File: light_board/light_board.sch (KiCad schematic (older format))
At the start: 15 parts, among them J1 CONN_01x02, Q1 PFET, U1 LM3409MY

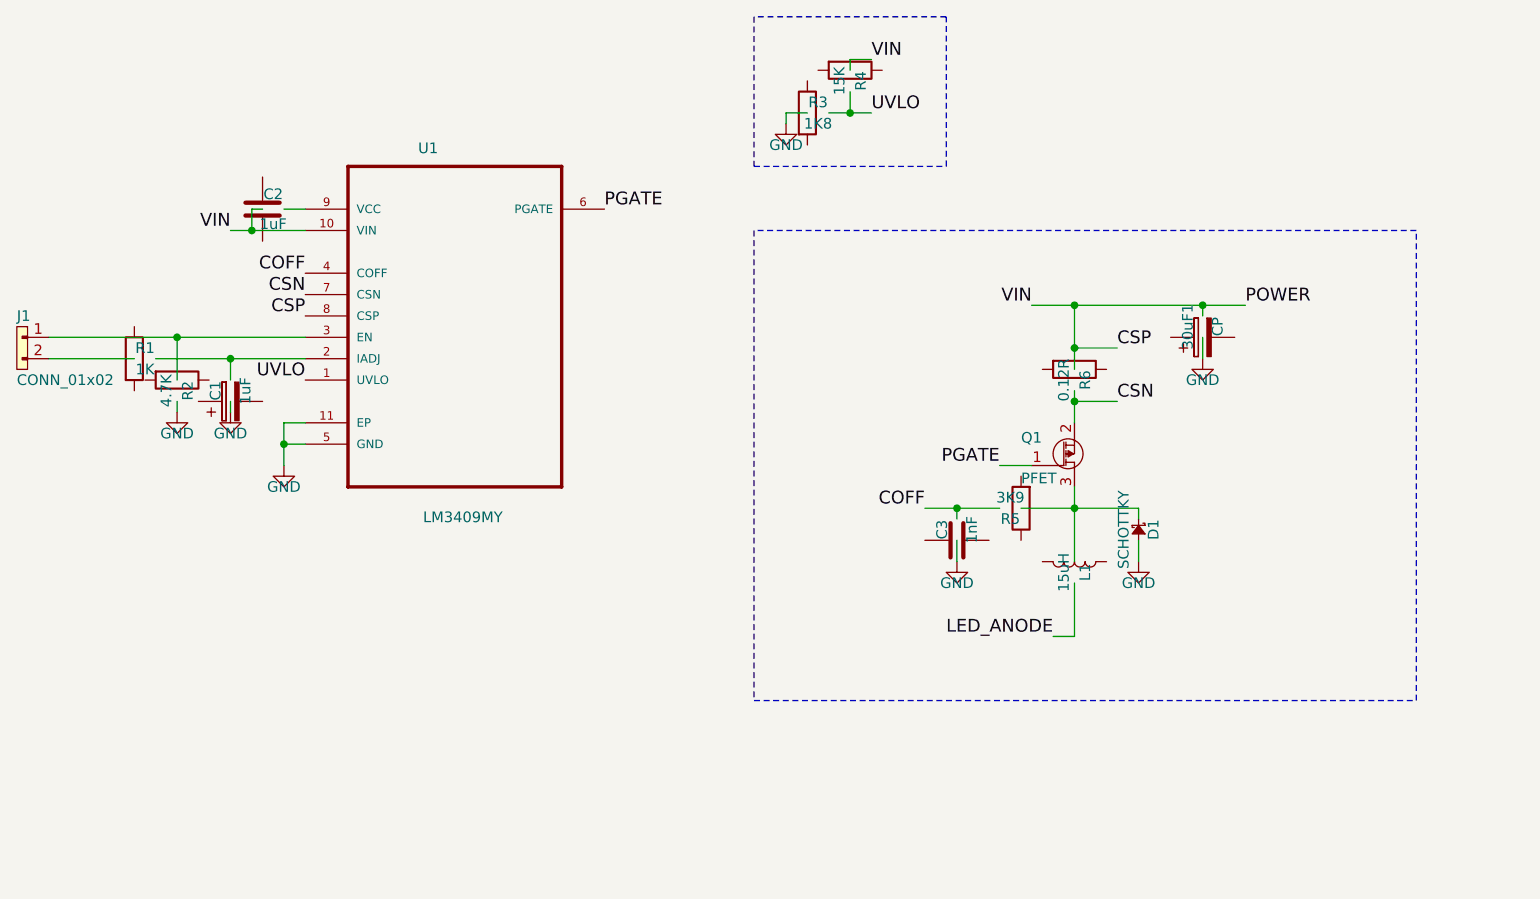
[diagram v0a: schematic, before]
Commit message: first version of light board, need to change resistor
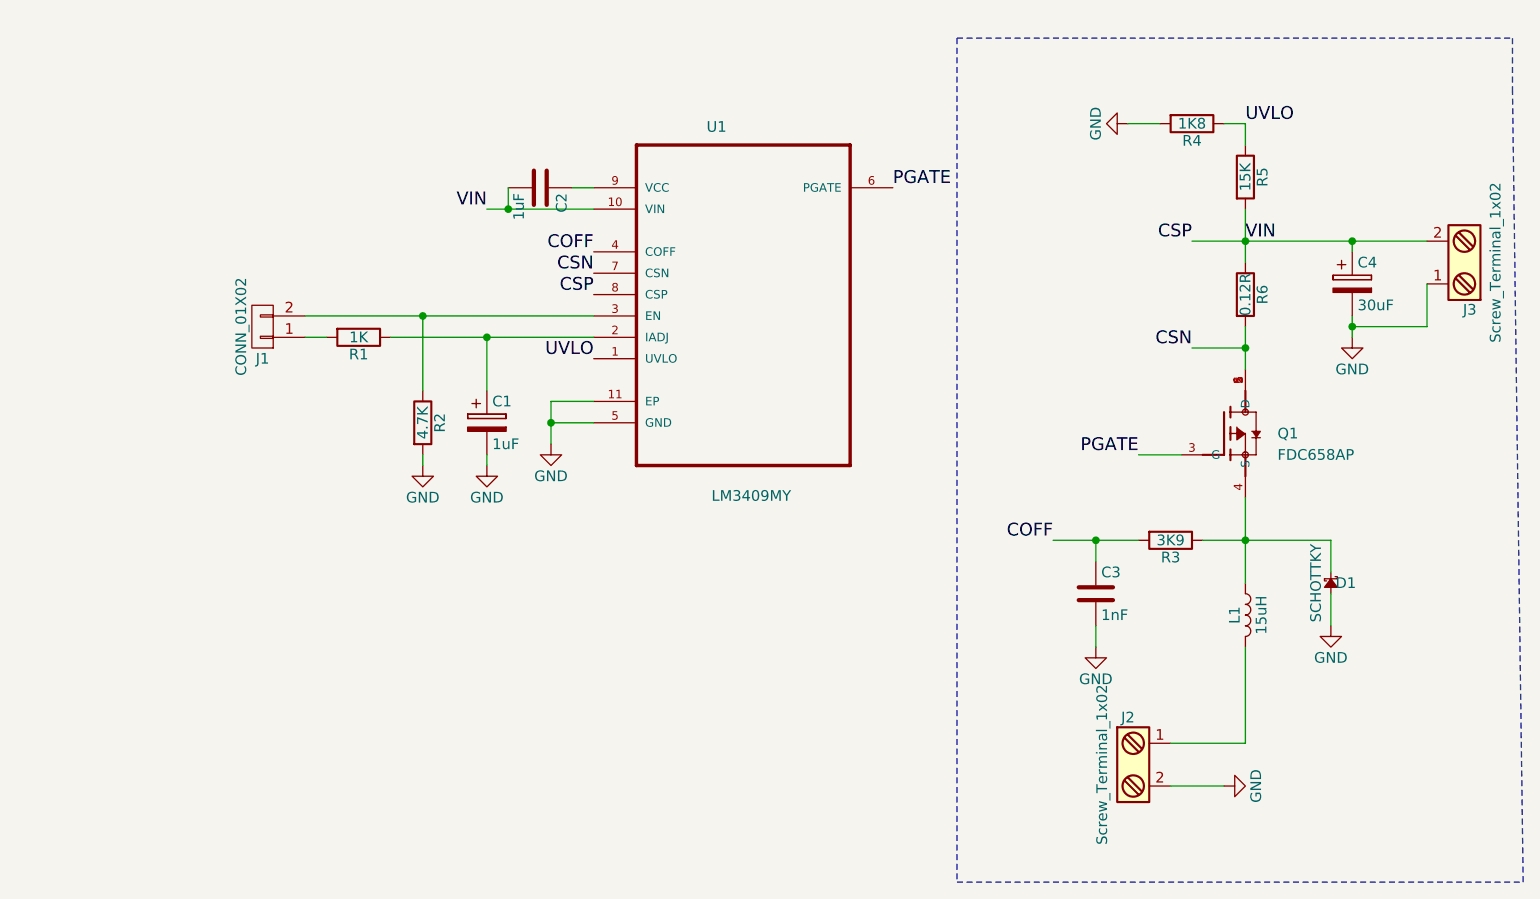
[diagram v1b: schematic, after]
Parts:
- removed 30uF1: CP, symbol CP
- removed J1: CONN_01x02, symbol CONN_01x02
- removed Q1: PFET, symbol PFET
- added C4: 30uF, Capacitors_THT:CP_Radial_Tantal_D5.0mm_P2.50mm, symbol CP
- added J1: CONN_01X02, Pin_Headers:Pin_Header_Straight_1x02_Pitch2.54mm, symbol CONN_01X02
- added J2, J3: Screw_Terminal_1x02, footprints:POWER_CONN, symbol Screw_Terminal_1x02
- added Q1: FDC658AP, footprints:FDC658AP FDC658AP, symbol FDC658AP
- C1: footprint (none) -> Capacitors_THT:CP_Radial_Tantal_D5.0mm_P2.50mm
- C2, C3, R1, R2, R6: footprint (none) -> agg:0805
- D1: footprint (none) -> Diodes_THT:D_5KPW_P7.62mm_Vertical_AnodeUp
- L1: footprint (none) -> Inductors_THT:L_Axial_L16.0mm_D6.3mm_P25.40mm_Horizontal_Fastron_VHBCC
- R3: value 1K8 -> 3K9; footprint (none) -> agg:0805
- R4: value 15K -> 1K8; footprint (none) -> agg:0805
- R5: value 3K9 -> 15K; footprint (none) -> agg:0805
- U1: footprint SOP50P490X109-11N -> footprints:LM3409
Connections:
- net labels removed: LED_ANODE, POWER
- wire segments 37 -> 35
